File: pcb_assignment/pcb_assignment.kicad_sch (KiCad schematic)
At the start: 54 parts, among them J1 Conn_01x02, J2 Conn_01x04, J3 Conn_01x04, J4 USB_C_Receptacle, SW1 SW_Push, T1 Transformer_1P_SS, U1 LP2985-3.3, U2 ESP32-WROOM-32, U3 DW1000-I-TR13, X1 38.4MHz

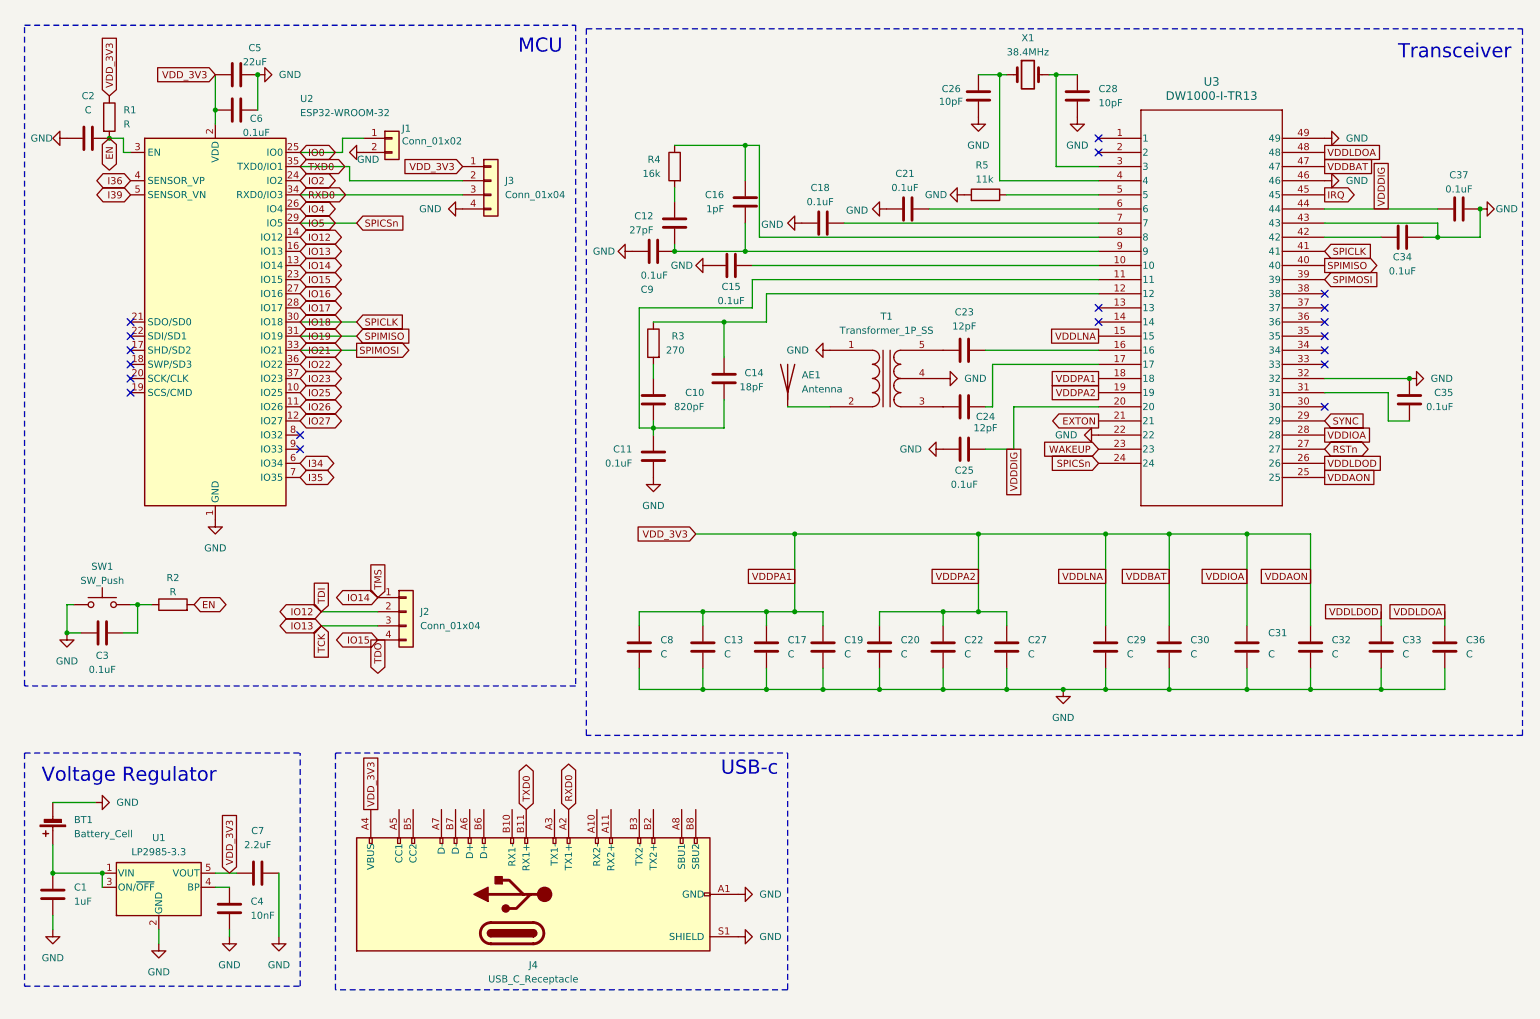
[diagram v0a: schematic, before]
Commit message: Finished schematic and pcb design, added gerber files, edited changelog
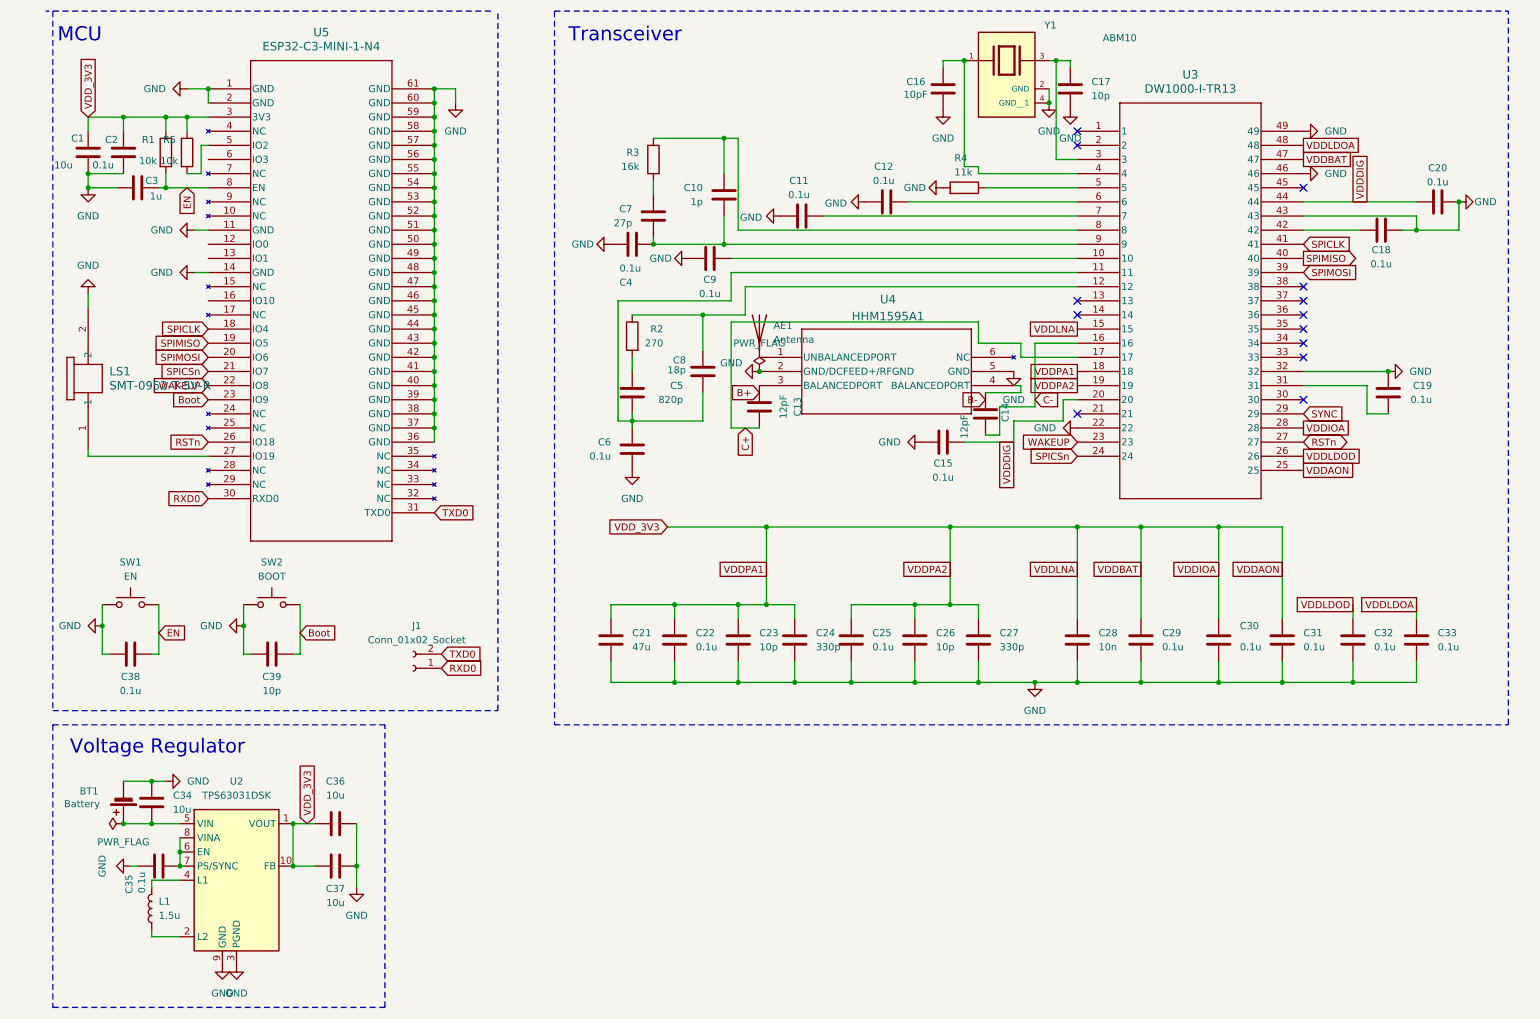
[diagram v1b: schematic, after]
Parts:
- removed J1: Conn_01x02, symbol Connector_Generic:Conn_01x02
- removed J2, J3: Conn_01x04, symbol Connector_Generic:Conn_01x04
- removed J4: USB_C_Receptacle, symbol Connector:USB_C_Receptacle
- removed T1: Transformer_1P_SS, symbol Device:Transformer_1P_SS
- removed U1: LP2985-3.3, Package_TO_SOT_SMD:SOT-23-5, symbol Regulator_Linear:LP2985-3.3
- removed U2: ESP32-WROOM-32, RF_Module:ESP32-WROOM-32, symbol RF_Module:ESP32-WROOM-32
- removed X1: 38.4MHz, symbol Device:Crystal
- added C38: 0.1u, Capacitor_SMD:C_0402_1005Metric, symbol Device:C
- added C39: 10p, Capacitor_SMD:C_0402_1005Metric, symbol Device:C
- added J1: Conn_01x02_Socket, Connector_PinHeader_2.00mm:PinHeader_1x02_P2.00mm_Horizontal, symbol Connector:Conn_01x02_Socket
- added L1: 1.5u, Inductor_SMD:L_Taiyo-Yuden_NR-30xx, symbol Device:L
- added LS1: SMT-0952-T-5V-R, SMT-0952-T-5V-R:SMT-0952-T-5V-R_PUI, symbol SMT-0952-T-5V-R:SMT-0952-T-5V-R
- added SW2: BOOT, Button_Switch_THT:SW_PUSH_6mm, symbol Switch:SW_Push
- added U2: TPS63031DSK, Package_SON:WSON-10-1EP_2.5x2.5mm_P0.5mm_EP1.2x2mm, symbol Regulator_Switching:TPS63031DSK
- added U4: HHM1595A1, HHM1595A1:HHM-6_2P0X1P25, symbol HHM1595A1:HHM1595A1
- added U5: ESP32-C3-MINI-1-N4, ESP32-C3-MINI-1_EXP, symbol ESP32-C3-MINI:ESP32-C3-MINI-1-N4
- added Y1: ABM10, ABM10_165_38:XTAL_ABM10-165-38.400MHZ-T3, symbol ABM10-165-38:ABM10-165-38.400MHZ-T3
- AE1: footprint (none) -> AH086M555003:AH086M_TAY
- BT1: value Battery_Cell -> Battery; footprint (none) -> Connector_JST:JST_ACH_BM02B-ACHSS-GAN-ETF_1x02-1MP_P1.20mm_Vertical
- C1: value 1uF -> 10u; footprint (none) -> Capacitor_SMD:C_0402_1005Metric
- C10: value 820pF -> 1p; footprint (none) -> Capacitor_SMD:C_0402_1005Metric
- C11, C15, C18, C25, C35, C6, C9: value 0.1uF -> 0.1u; footprint (none) -> Capacitor_SMD:C_0402_1005Metric
- C12: value 27pF -> 0.1u; footprint (none) -> Capacitor_SMD:C_0402_1005Metric
- C13: value C -> 12pF; footprint (none) -> Capacitor_SMD:C_0402_1005Metric
- C14: value 18pF -> 12pF; footprint (none) -> Capacitor_SMD:C_0402_1005Metric
- C16: value 1pF -> 10pF; footprint (none) -> Capacitor_SMD:C_0402_1005Metric
- C17: value C -> 10p; footprint (none) -> Capacitor_SMD:C_0402_1005Metric
- C19, C2, C20, C22, C29, C30, C31, C32, C33: value C -> 0.1u; footprint (none) -> Capacitor_SMD:C_0402_1005Metric
- C21: value 0.1uF -> 47u; footprint (none) -> Capacitor_SMD:C_0402_1005Metric
- C23: value 12pF -> 10p; footprint (none) -> Capacitor_SMD:C_0402_1005Metric
- C24: value 12pF -> 330p; footprint (none) -> Capacitor_SMD:C_0402_1005Metric
- C26: value 10pF -> 10p; footprint (none) -> Capacitor_SMD:C_0402_1005Metric
- C27: value C -> 330p; footprint (none) -> Capacitor_SMD:C_0402_1005Metric
- C28: value 10pF -> 10n; footprint (none) -> Capacitor_SMD:C_0402_1005Metric
- C3: value 0.1uF -> 1u; footprint (none) -> Capacitor_SMD:C_0402_1005Metric
- C34, C37: value 0.1uF -> 10u; footprint (none) -> Capacitor_SMD:C_0402_1005Metric
- C36: value C -> 10u; footprint (none) -> Capacitor_SMD:C_0402_1005Metric
- C4: value 10nF -> 0.1u; footprint (none) -> Capacitor_SMD:C_0402_1005Metric
- C5: value 22uF -> 820p; footprint (none) -> Capacitor_SMD:C_0402_1005Metric
- C7: value 2.2uF -> 27p; footprint (none) -> Capacitor_SMD:C_0402_1005Metric
- C8: value C -> 18p; footprint (none) -> Capacitor_SMD:C_0402_1005Metric
- R1: value R -> 10k; footprint (none) -> Resistor_SMD:R_0402_1005Metric
- R2: value R -> 270; footprint (none) -> Resistor_SMD:R_0402_1005Metric
- R3: value 270 -> 16k; footprint (none) -> Resistor_SMD:R_0402_1005Metric
- R4: value 16k -> 11k; footprint (none) -> Resistor_SMD:R_0402_1005Metric
- R5: value 11k -> 10k; footprint (none) -> Resistor_SMD:R_0402_1005Metric
- SW1: value SW_Push -> EN; footprint (none) -> Button_Switch_THT:SW_PUSH_6mm
- U3: footprint VFQFN48_12X12_QOR -> DW1000:VFQFN48_12X12_QOR
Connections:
- net EN: now also C3.2, SW1.2, C38.2, U5.8 (EN); no longer C2.2, R2.2
- net GND: now also C12.2, C15.1, C16.2, C19.1, C2.2, C23.2, C24.2, C25.2, C34.1, C35.2, R4.2, C38.1, C39.1, LS1.2, SW2.1, U2.11 (PGND), U2.3 (PGND), U2.9 (GND), U4.2 (GND/DCFEED+/RFGND), U4.5 (GND), U5.1 (GND), U5.11 (GND), U5.14 (GND), U5.2 (GND), U5.36 (GND), U5.37 (GND), U5.38 (GND), U5.39 (GND), U5.40 (GND), U5.41 (GND), U5.42 (GND), U5.43 (GND), U5.44 (GND), U5.45 (GND), U5.46 (GND), U5.47 (GND), U5.48 (GND), U5.49 (GND), U5.50 (GND), U5.51 (GND), U5.52 (GND), U5.53 (GND), U5.54 (GND), U5.55 (GND), U5.56 (GND), U5.57 (GND), U5.58 (GND), U5.59 (GND), U5.60 (GND), U5.61 (GND), Y1.2 (GND), Y1.4 (GND__1); no longer C13.2, C15.2, C19.2, C2.1, C25.1, C34.2, C35.1, C5.2, C7.2, C8.2, R5.2
- net RSTn: now also U5.26 (IO18)
- net RXD0: now also J1.1 (Pin_1), U5.30 (RXD0)
- net TXD0: now also J1.2 (Pin_2), U5.31 (TXD0)
- net VDDAON: now also C1.1, C2.1, C21.1, C23.1, C24.1, C25.1, C26.1, C28.1, C36.1, C37.1, R5.1, U2.1 (VOUT), U2.10 (FB), U5.3 (3V3); no longer C13.1, C17.1, C19.1, C20.1, C32.1, C5.1, C6.1, C7.1, C8.1
- net VDDDIG: now also C15.2, C20.1; no longer C25.2, C37.1
- net VDDLDOA: now also C33.1; no longer C36.1
- net VDDLDOD: now also C32.1; no longer C33.1
- net WAKEUP: now also U5.22 (IO8)
- net C+: now reaches U3.17
- net C+: now also C13.2; no longer C24.2
- net at C12.1: now also U3.6; no longer R4.2
- net at C18.1: now also U3.42; no longer U3.7
- net at U3.3: now also C17.1, Y1.3; no longer C28.1
- net at U3.4: now also C16.1, Y1.1; no longer C26.1
- net C-: now reaches U3.16
- net C-: now also C14.2; no longer C23.2
- net at C10.1: now also R3.1, U3.8; no longer R3.2
- net at U3.10: now also C9.1; no longer C15.1
- net at U3.31: now also C19.2; no longer C35.2
- net at U3.5: now also R4.1; no longer R5.1
- net at BT1.1 (+): now also C34.2, U2.5 (VIN); no longer C1.1
- net at C4.1: now also C10.2, C7.2, U3.9
- net at AE1.1 (A): now also U4.1 (UNBALANCEDPORT)
- net EXTON: no longer names the net of U3.21
- net IO18 renamed SPICLK
- net SPICLK: now also U5.18 (IO4)
- net IO19 renamed SPIMISO
- net SPIMISO: now also U5.19 (IO5)
- net IO21 renamed SPIMOSI
- net SPIMOSI: now also U5.20 (IO6)
- net IO5 renamed SPICSn
- net SPICSn: now also U5.21 (IO7)
- net IRQ: no longer names the net of U3.45
- new net: C5.2, C6.1, C8.2, U3.11
- new net: C8.1, R2.1, U3.12
- new net: C11.1, U3.7
- new net: L1.1, U2.2 (L2)
- new net: L1.2, U2.4 (L1)
- new net: C5.1, R2.2
- new net: C35.1, U2.6 (EN), U2.7 (PS/SYNC), U2.8 (VINA)
- new net: C13.1, U4.3 (BALANCEDPORT)
- new net: C14.1, U4.4 (BALANCEDPORT)
- new net: LS1.1, U5.27 (IO19)
- new net: C7.1, R3.2
- new net: R5.2, U5.5 (IO2)
- new net Boot: C39.2, SW2.2, U5.23 (IO9)
- no-connect marks 19 -> 13
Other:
- note removed: "USB-c"
